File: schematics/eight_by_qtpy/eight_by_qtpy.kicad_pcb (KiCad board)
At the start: 2 copper layers, 198.9 x 48.4 mm, 53 parts, among them J1 Conn_01x08, J2 AudioJack4, SW1 TC-1103-C-D, SW10 TC-1103-C-D, SW2 TC-1103-C-D, SW3 TC-1103-C-D, SW4 TC-1103-C-D, SW5 TC-1103-C-D, SW6 TC-1103-C-D, SW7 TC-1103-C-D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

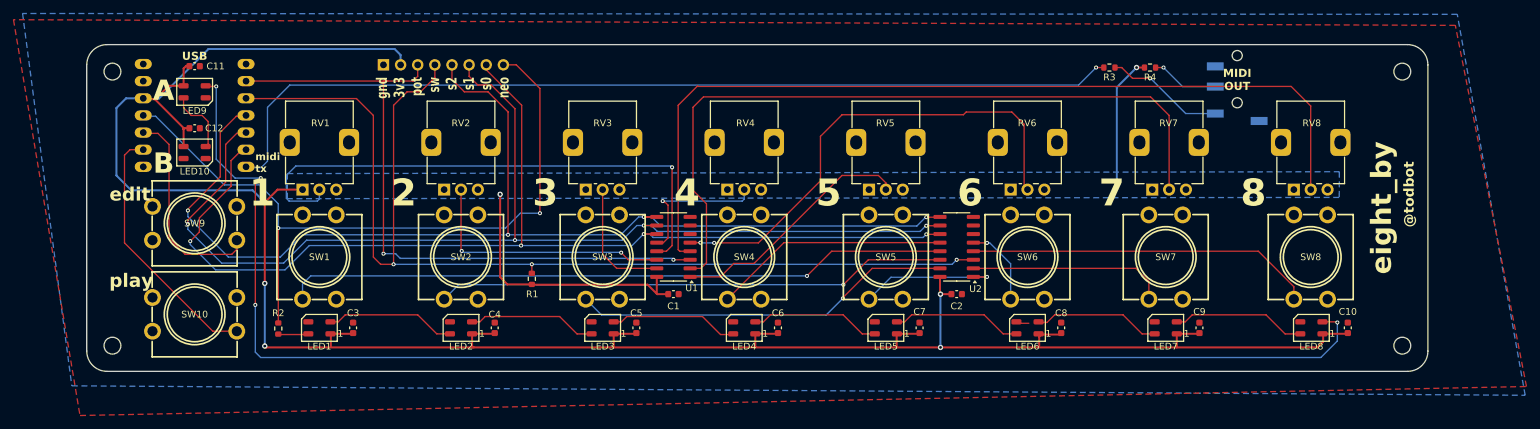
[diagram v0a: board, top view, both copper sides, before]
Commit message: clean up eight_by_qtpy refactor layout
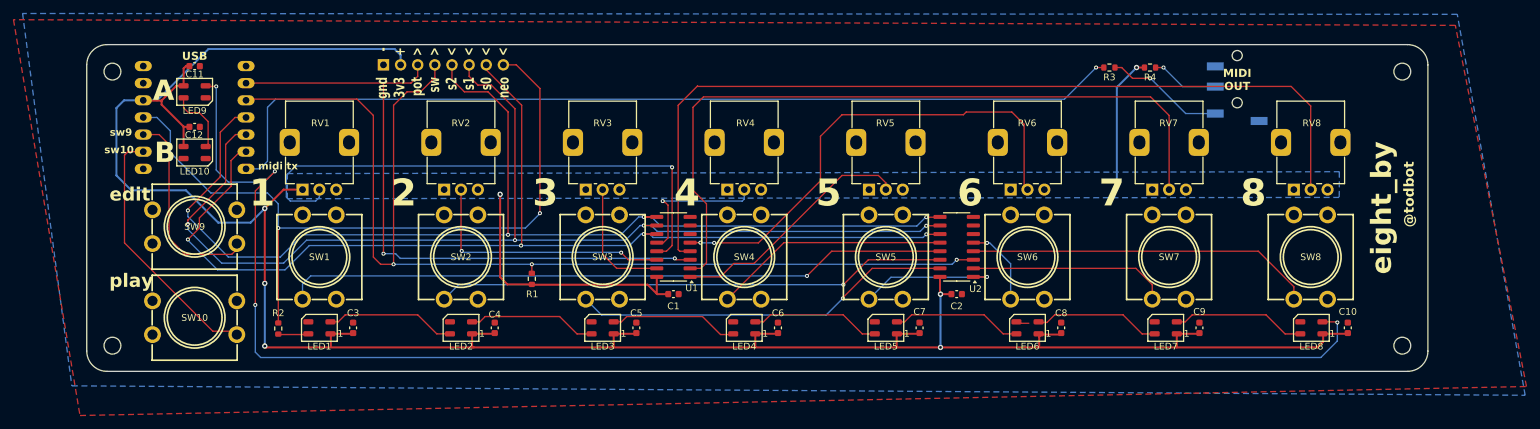
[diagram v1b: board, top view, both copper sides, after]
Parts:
- moved SW10 0.50 mm to (41.4, 61.9)
- moved SW7 0.50 mm to (185.9, 52.9)
- moved SW9 0.50 mm to (41.4, 48.4)
- moved U3 0.30 mm to (41.4, 32.2)
- moved C12 0.20 mm to (41.4, 33.6)
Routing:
- net Net-(LED8-DOUT): track 213.0 -> 218.8 mm
- net /NEOPIXEL: track 107.6 -> 110.0 mm
- net +3V3: track 399.5 -> 401.7 mm
- net /MIDI_OUT: track 137.4 -> 138.1 mm
- net /S2: track 172.1 -> 171.4 mm
- net /S1: track 167.9 -> 167.2 mm
- net /SW: track 164.7 -> 165.3 mm
- net /S0: track 164.7 -> 164.1 mm
- net /SW9: track 30.0 -> 30.5 mm
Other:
- board text added: "- + > > < < < <"
- board text added: "10"
- board text added: "9"
- board text added: "sw10"
- board text added: "sw9"

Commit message: files as sent to fab
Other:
- board text added: "JLCJLCJLCJLC"
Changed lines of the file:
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@@
+		)
+	)
+	(gr_text "JLCJLCJLCJLC"
+		(at 211.4 66 0)
+		(layer "B.SilkS")
+		(effects
+			(font
+				(size 1.2 1.2)
+				(thickness 0.2)
+				(bold yes)
+			)
+			(justify mirror)
 		)
 	)
